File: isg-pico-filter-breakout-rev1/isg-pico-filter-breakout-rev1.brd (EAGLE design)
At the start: 91.4 x 66 mm, 51 parts, among them IC1 PICO_BAREDIE, U1 OPA2380AIDGKT, U2 OPA2380AIDGKT, U3 OPA2380AIDGKT, U4 OPA2380AIDGKT, U5 OPA2380AIDGKT, X3 PD_BIAS_N

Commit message: work on TIA layout
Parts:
- removed X3: PD_BIAS_N, con-coax:J502-ND-142-0701-881/886
- added JP1: (no value), pinhead:2X10
- added JP2: TIA_OUT, pinhead:2X10
- added R21, R22, R23, R24, R25, R26, R27, R28, R29, R30: RES SMD 49.9 OHM 1% 0603, rcl-modified-footprints:R0603
- added X1, X2: 1365-20, con-leotronics:1365-20
- moved H1 25.4 mm to (61.0, 19.1)
- moved H3 25.4 mm to (61.0, 47.0)
- moved H6 25.4 mm to (58.4, 7.62)
- moved H7 25.4 mm to (58.4, 58.4)
- moved R12 16.6 mm to (16.8, 56.2), turned to 270 degrees
- moved R11 16.2 mm to (16.8, 45.4), turned to 90 degrees
- moved R14 15.9 mm to (23.8, 56.2), turned to 270 degrees
- moved R13 15.6 mm to (23.8, 45.4), turned to 90 degrees
- moved R16 15.3 mm to (30.8, 56.2), turned to 270 degrees
- moved R15 15.0 mm to (30.8, 45.4), turned to 90 degrees
- moved R18 14.7 mm to (37.8, 56.2), turned to 270 degrees
- moved R17 14.3 mm to (37.8, 45.4), turned to 90 degrees
- moved R20 14.1 mm to (44.8, 56.2), turned to 270 degrees
- moved R1 14.1 mm to (19.1, 44.5)
- moved C1 14.0 mm to (19.1, 46.4)
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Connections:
- new net +5V: C12.1, C15.1, C3.1, C6.1, C9.1, JP1.19, U1.8, U2.8, U3.8, U4.8, U5.8
- new net -5V: JP1.1, R11.2, R12.2, R13.2, R14.2, R15.2, R16.2, R17.2, R18.2, R19.2, R20.2
- new net N$1: IC1.F1_H1_A, JP1.20
- new net N$10: IC1.F4_H1_A, JP1.2
- new net N$11: C4.2, R13.1, R23.1, R3.2, U2.1
- new net N$12: JP2.19, R21.2
- new net N$13: JP2.17, R22.2
- new net N$14: JP2.15, R23.2
- new net N$15: JP2.13, R24.2
- new net N$16: JP2.11, R25.2
- new net N$17: JP2.9, R26.2
- new net N$18: JP2.7, R27.2
- new net N$19: JP2.5, R28.2
- new net N$20: JP2.3, R29.2
- new net N$21: JP2.1, R30.2
- new net N$8: IC1.F4_H3_A, JP1.6
- new net N$9: IC1.F4_H2_A, JP1.4
- net F1_PD1_VOUT: now also R21.1
- net F2_PD1_VOUT: now also R22.1; no longer C4.2, R13.1, R3.2, U2.1
- net F3_PD1_VOUT: now also R26.1
- net F3_PD2_VOUT: now also R25.1
- net F3_PD3_VOUT: now also R24.1
- net F4_PD1_VOUT: now also R30.1
- net F4_PD2_VOUT: now also R29.1
- net F4_PD3_VOUT: now also R28.1
- net F4_PD4_VOUT: now also R27.1
- net GND: now also IC1.F1_H1_B, IC1.F2_H1_B, IC1.F2_H2_B, IC1.F3_H1_B, IC1.F3_H2_B, IC1.F3_H3_B, IC1.F4_H1_B, IC1.F4_H2_B, IC1.F4_H3_B, IC1.F4_H4_B, JP1.11, JP1.13, JP1.15, JP1.17, JP1.3, JP1.5, JP1.7, JP1.9, JP2.10, JP2.12, JP2.14, JP2.16, JP2.18, JP2.2, JP2.20, JP2.4, JP2.6, JP2.8; no longer X3.G@1, X3.G@2, X3.G@3, X3.G@4
- net N$2: now also IC1.F2_H2_A, JP1.18; no longer R11.2, R12.2
- net N$3: now also IC1.F2_H1_A, JP1.16; no longer R13.2, R14.2
- net N$4: now also IC1.F3_H3_A, JP1.14; no longer R15.2, R16.2
- net N$5: now also IC1.F3_H2_A, JP1.12; no longer R17.2, R18.2
- net N$6: now also IC1.F3_H1_A, JP1.10; no longer C12.1, C15.1, C3.1, C6.1, C9.1, U1.8, U2.8, U3.8, U4.8, U5.8
- net N$7: now also IC1.F4_H4_A, JP1.8; no longer R19.2, R20.2
- net PD_BIAS_N: no longer X3.1
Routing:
- net N$10: track 0.00 -> 24.3 mm
- net N$1: track 0.00 -> 24.0 mm
- net N$9: track 0.00 -> 23.3 mm
- net N$2: track 0.00 -> 23.0 mm
- net N$8: track 0.00 -> 22.4 mm
- net N$3: track 0.00 -> 22.1 mm
- net N$7: track 0.00 -> 21.5 mm
- net N$4: track 0.00 -> 21.5 mm
- net N$12: track 0.00 -> 21.1 mm
- net N$5: track 0.00 -> 20.6 mm
- net N$14: track 0.00 -> 19.2 mm
- net N$16: track 0.00 -> 17.3 mm
- net N$18: track 0.00 -> 16.1 mm
- net N$20: track 0.00 -> 15.4 mm
- net +5V: track 0.00 -> 14.3 mm
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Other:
- board size 91.4 x 66 mm -> 66 x 66 mm

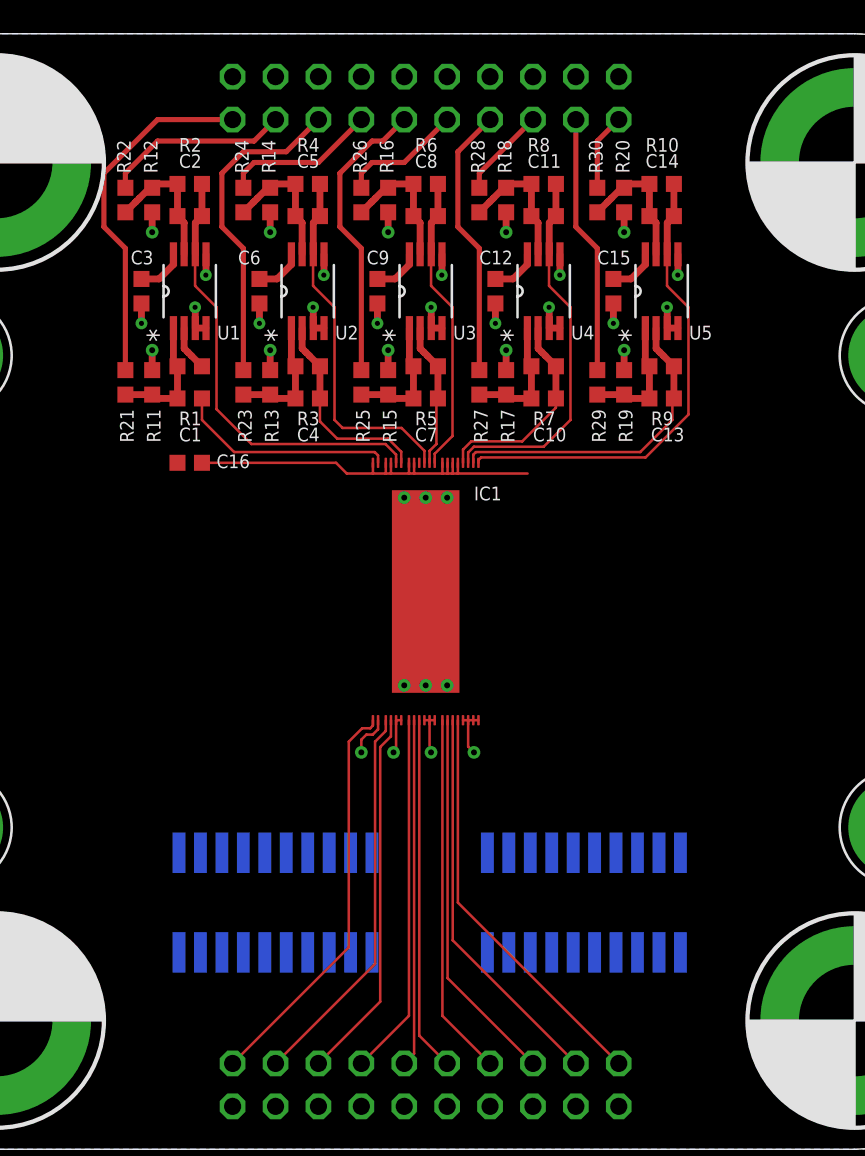
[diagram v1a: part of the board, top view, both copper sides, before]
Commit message: TIAs routed to 0.1" header
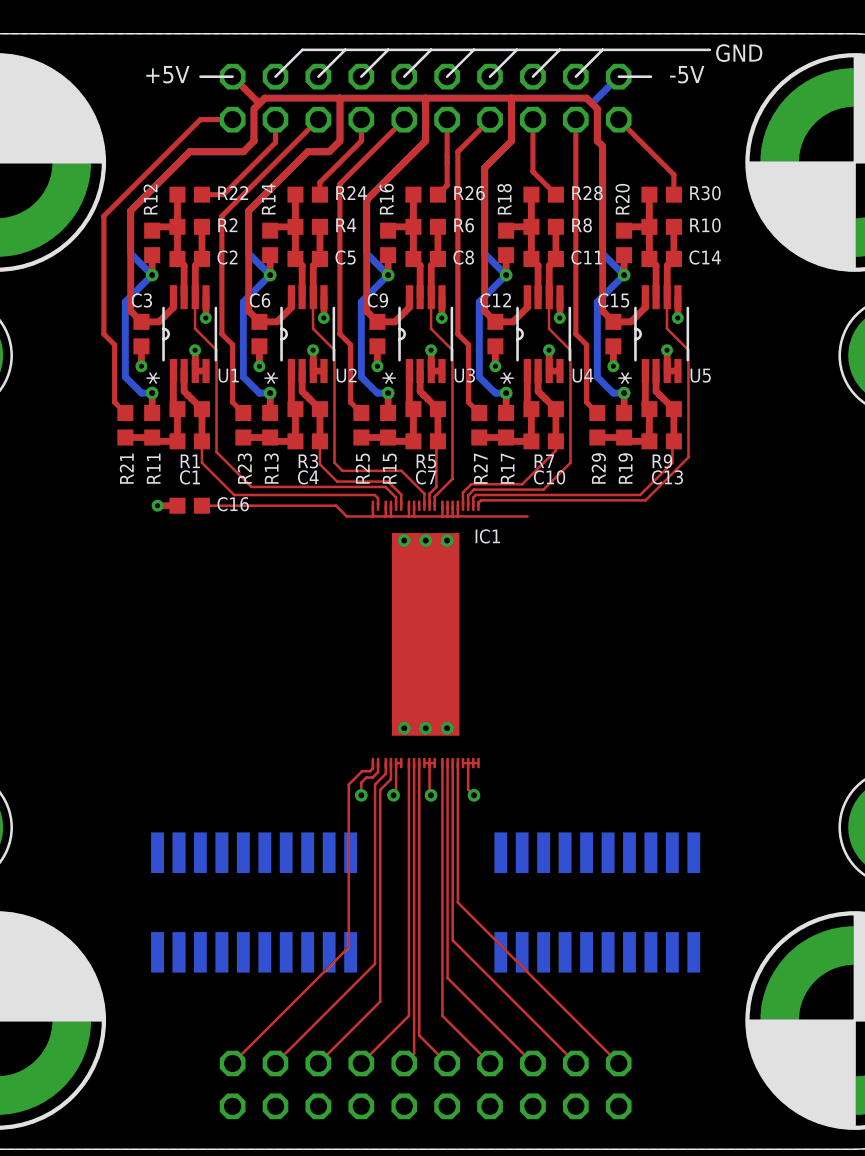
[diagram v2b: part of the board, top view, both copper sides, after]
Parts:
- moved R26 3.82 mm to (33.0, 56.5), turned to 0 degrees
- moved R28 3.82 mm to (40.0, 56.5), turned to 0 degrees
- moved R30 3.82 mm to (47.0, 56.5), turned to 0 degrees
- moved R22 3.82 mm to (19.1, 56.5), turned to 0 degrees
- moved R24 3.82 mm to (26.0, 56.5), turned to 0 degrees
- moved R1 2.54 mm to (19.1, 41.9)
- moved R11 2.54 mm to (16.8, 42.9)
- moved R13 2.54 mm to (23.8, 42.9)
- moved R15 2.54 mm to (30.8, 42.9)
- moved R17 2.54 mm to (37.8, 42.9)
- moved R19 2.54 mm to (44.8, 42.9)
- moved R21 2.54 mm to (15.2, 42.9)
- moved R23 2.54 mm to (22.2, 42.9)
- moved R25 2.54 mm to (29.2, 42.9)
- moved R27 2.54 mm to (36.2, 42.9)
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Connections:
- net N$12 renamed F1_PD1_VOUT_R
- net N$13 renamed F2_PD2_VOUT_R
- net N$14 renamed F2_PD1_VOUT_R
- net N$15 renamed F3_PD3_VOUT_R
- net N$16 renamed F3_PD2_VOUT_R
- net N$17 renamed F3_PD1_VOUT_R
- net N$18 renamed F4_PD4_VOUT_R
- net N$19 renamed F4_PD3_VOUT_R
- net N$20 renamed F4_PD2_VOUT_R
- net N$21 renamed F4_PD1_VOUT_R
- removed net N$11: C4.2, R13.1, R23.1, R3.2, U2.1
- new net F2_PD2_VOUT: C2.2, R12.1, R2.2, R22.1, U1.7
- net +5V: now also JP2.20; no longer JP1.19
- net -5V: now also JP2.2; no longer JP1.1
- net F2_PD1_VOUT: now also C4.2, R13.1, R23.1, R3.2, U2.1; no longer C2.2, R12.1, R2.2, R22.1, U1.7
- net GND: no longer JP2.2, JP2.20
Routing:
- net -5V: track 11.8 -> 142.1 mm
- net +5V: track 14.3 -> 113.7 mm
- net F2_PD2_VOUT: track 0.00 -> 7.96 mm
- net N$11: track 7.44 -> 0.00 mm
- net F2_PD2_VOUT_R: track 11.1 -> 6.99 mm
- net F3_PD3_VOUT_R: track 9.16 -> 5.46 mm
- net F3_PD1_VOUT_R: track 7.26 -> 4.67 mm
- net N$9: track 23.3 -> 20.8 mm
- net N$8: track 22.4 -> 19.9 mm
- net N$7: track 21.5 -> 18.9 mm
- net N$6: track 21.0 -> 18.5 mm
- net N$5: track 20.6 -> 18.0 mm
- net N$4: track 21.5 -> 18.9 mm
- net N$3: track 22.1 -> 19.6 mm
- net N$2: track 23.0 -> 20.5 mm
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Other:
- board text added: "+5V"
- board text added: "-5V"
- board text added: "GND"

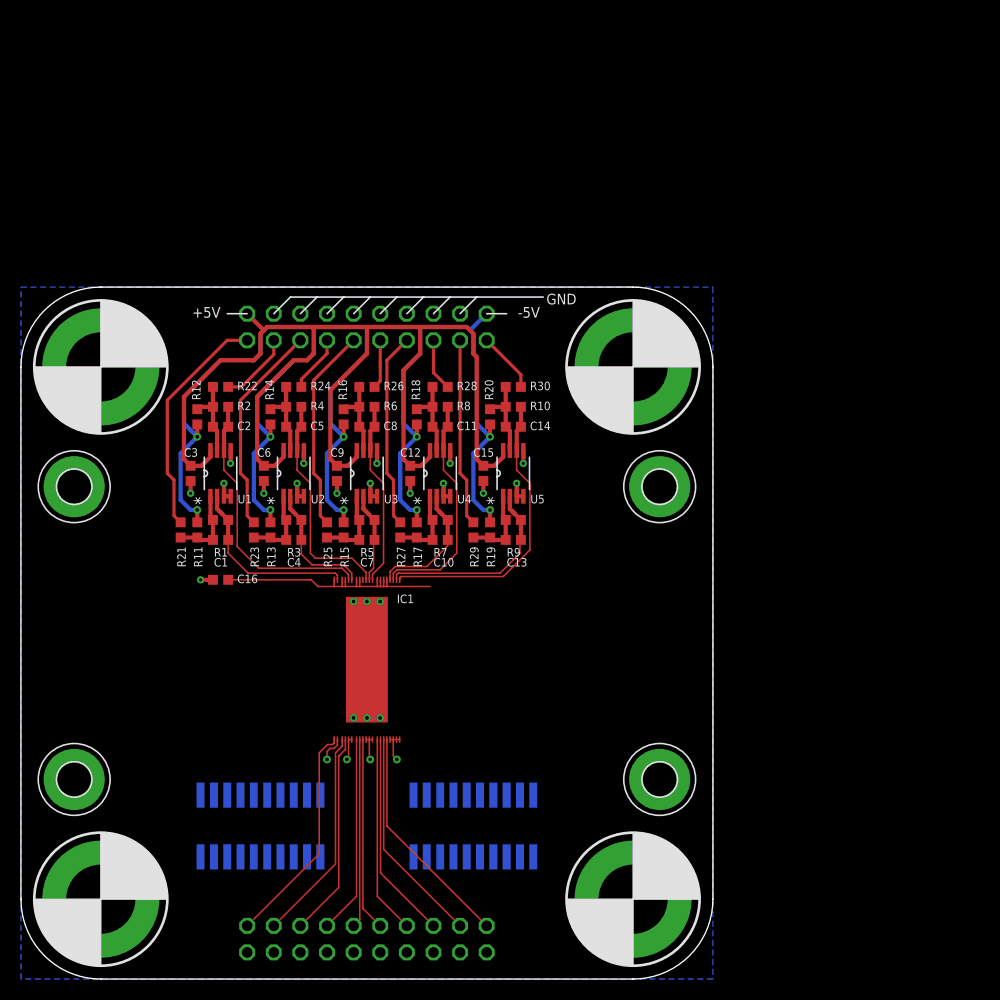
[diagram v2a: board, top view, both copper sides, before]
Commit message: first-pass routing done
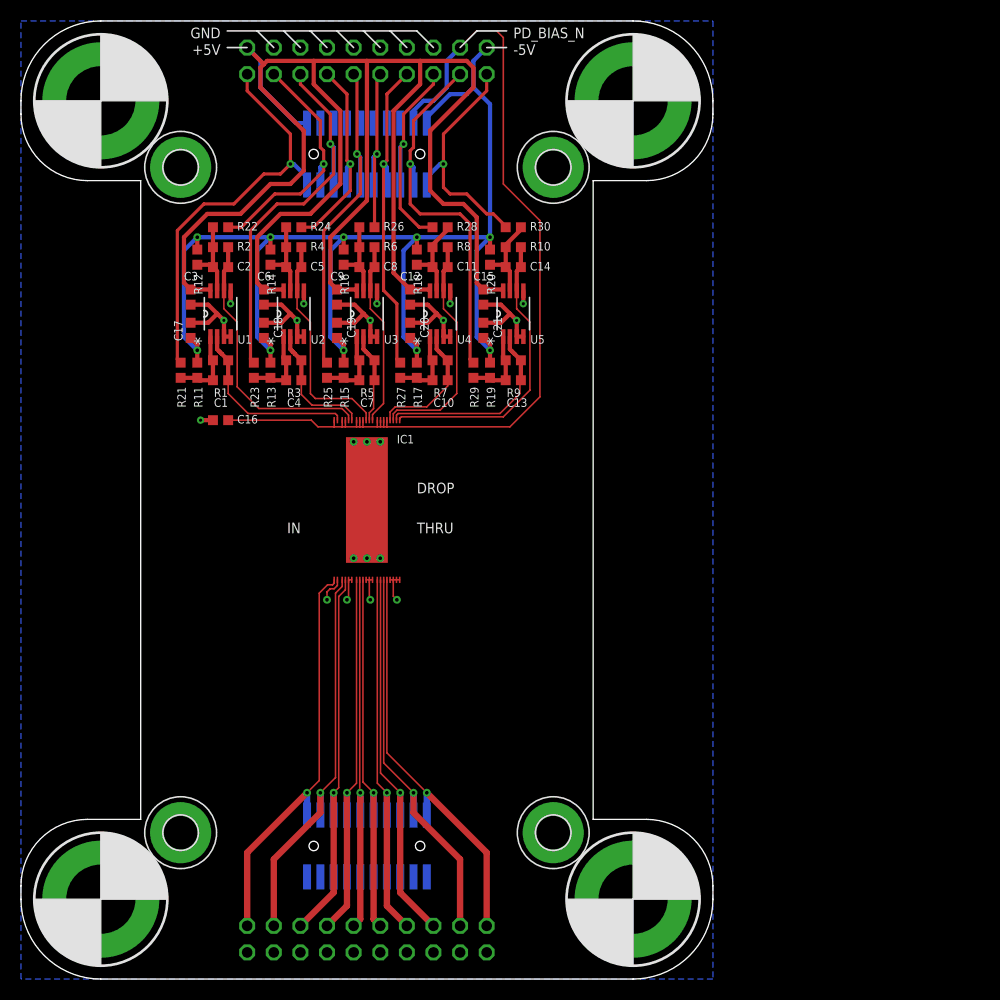
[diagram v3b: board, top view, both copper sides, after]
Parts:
- removed X1, X2: 1365-20, con-leotronics:1365-20
- added C17, C18, C19, C20, C21: CAP CER 0.1UF X7R 0603, rcl-modified-footprints:C0603
- added JP3, JP4: HEATERS, isg-custom:FTSH-110-01-L-DV-K-TR
- C12, C15, C16, C3, C6, C9: value CAP CER 100NF X7R 0603 -> CAP CER 0.1UF X7R 0603
- JP1: value (none) -> HEATERS
- moved H3 32.1 mm to (50.8, 77.5)
- moved H4 32.1 mm to (15.2, 77.5)
- moved JP2 25.4 mm to (33.0, 87.6)
- moved H7 25.4 mm to (58.4, 83.8)
- moved H8 25.4 mm to (7.62, 83.8)
- moved C12 16.8 mm to (37.1, 65.1)
- moved C15 16.8 mm to (44.1, 65.1)
- moved C3 16.8 mm to (16.2, 65.1)
- moved C6 16.8 mm to (23.2, 65.1)
- moved C9 16.8 mm to (30.2, 65.1)
- moved C1 15.2 mm to (19.1, 59.1)
- moved C10 15.2 mm to (40.0, 59.1)
- moved C13 15.2 mm to (47.0, 59.1)
- moved C16 15.2 mm to (19.1, 53.3)
- moved C4 15.2 mm to (26.0, 59.1)
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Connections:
- removed net N$1: IC1.F1_H1_A, JP1.20
- removed net N$10: IC1.F4_H1_A, JP1.2
- removed net N$2: IC1.F2_H2_A, JP1.18
- removed net N$3: IC1.F2_H1_A, JP1.16
- removed net N$4: IC1.F3_H3_A, JP1.14
- removed net N$5: IC1.F3_H2_A, JP1.12
- removed net N$6: IC1.F3_H1_A, JP1.10
- removed net N$7: IC1.F4_H4_A, JP1.8
- removed net N$8: IC1.F4_H3_A, JP1.6
- removed net N$9: IC1.F4_H2_A, JP1.4
- new net F1_H1_A: IC1.F1_H1_A, JP1.20, JP4.20
- new net F2_H1_A: IC1.F2_H1_A, JP1.16, JP4.16
- new net F2_H2_A: IC1.F2_H2_A, JP1.18, JP4.18
- new net F3_H1_A: IC1.F3_H1_A, JP1.10, JP4.10
- new net F3_H2_A: IC1.F3_H2_A, JP1.12, JP4.12
- new net F3_H3_A: IC1.F3_H3_A, JP1.14, JP4.14
- new net F4_H1_A: IC1.F4_H1_A, JP1.2, JP4.2
- new net F4_H2_A: IC1.F4_H2_A, JP1.4, JP4.4
- new net F4_H3_A: IC1.F4_H3_A, JP1.6, JP4.6
- new net F4_H4_A: IC1.F4_H4_A, JP1.8, JP4.8
- net +5V: now also JP3.1
- net -5V: now also C17.2, C18.2, C19.2, C20.2, C21.2, JP3.19
- net F1_PD1_VOUT_R: now also JP3.2
- net F2_PD1_VOUT_R: now also JP3.6
- net F2_PD2_VOUT_R: now also JP3.4
- net F3_PD1_VOUT_R: now also JP3.12
- net F3_PD2_VOUT_R: now also JP3.10
- net F3_PD3_VOUT_R: now also JP3.8
- net F4_PD1_VOUT_R: now also JP3.20
- net F4_PD2_VOUT_R: now also JP3.18
- net F4_PD3_VOUT_R: now also JP3.16
- net F4_PD4_VOUT_R: now also JP3.14
- net GND: now also C17.1, C18.1, C19.1, C20.1, C21.1, JP1.1, JP1.19, JP3.11, JP3.13, JP3.15, JP3.3, JP3.5, JP3.7, JP3.9, JP4.1, JP4.11, JP4.13, JP4.15, JP4.17, JP4.19, JP4.3, JP4.5, JP4.7, JP4.9; no longer JP2.4
- net PD_BIAS_N: now also JP2.4, JP3.17
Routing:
- net PD_BIAS_N: track 25.3 -> 87.9 mm
- net +5V: track 113.7 -> 175.1 mm
- net F4_H1_A: track 0.00 -> 39.1 mm, vias 0 -> 1
- net F1_H1_A: track 0.00 -> 38.9 mm, vias 0 -> 1
- net F4_H2_A: track 0.00 -> 38.2 mm, vias 0 -> 1
- net F2_H2_A: track 0.00 -> 37.9 mm, vias 0 -> 1
- net F4_H3_A: track 0.00 -> 37.2 mm, vias 0 -> 1
- net F2_H1_A: track 0.00 -> 36.9 mm, vias 0 -> 1
- net F4_H4_A: track 0.00 -> 36.3 mm, vias 0 -> 1
- net F3_H3_A: track 0.00 -> 36.3 mm, vias 0 -> 1
- net F3_H1_A: track 0.00 -> 35.8 mm, vias 0 -> 1
- net F3_H2_A: track 0.00 -> 35.4 mm, vias 0 -> 1
- net GND: track 32.9 -> 67.7 mm, vias 26 -> 21
- net N$10: track 21.7 -> 0.00 mm
- net N$1: track 21.5 -> 0.00 mm
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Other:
- board size 66 x 66 mm -> 66 x 91.4 mm
- board text added: "DROP"
- board text added: "IN"
- board text added: "PD_BIAS_N"
- board text added: "THRU"

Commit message: Added ESD diodes
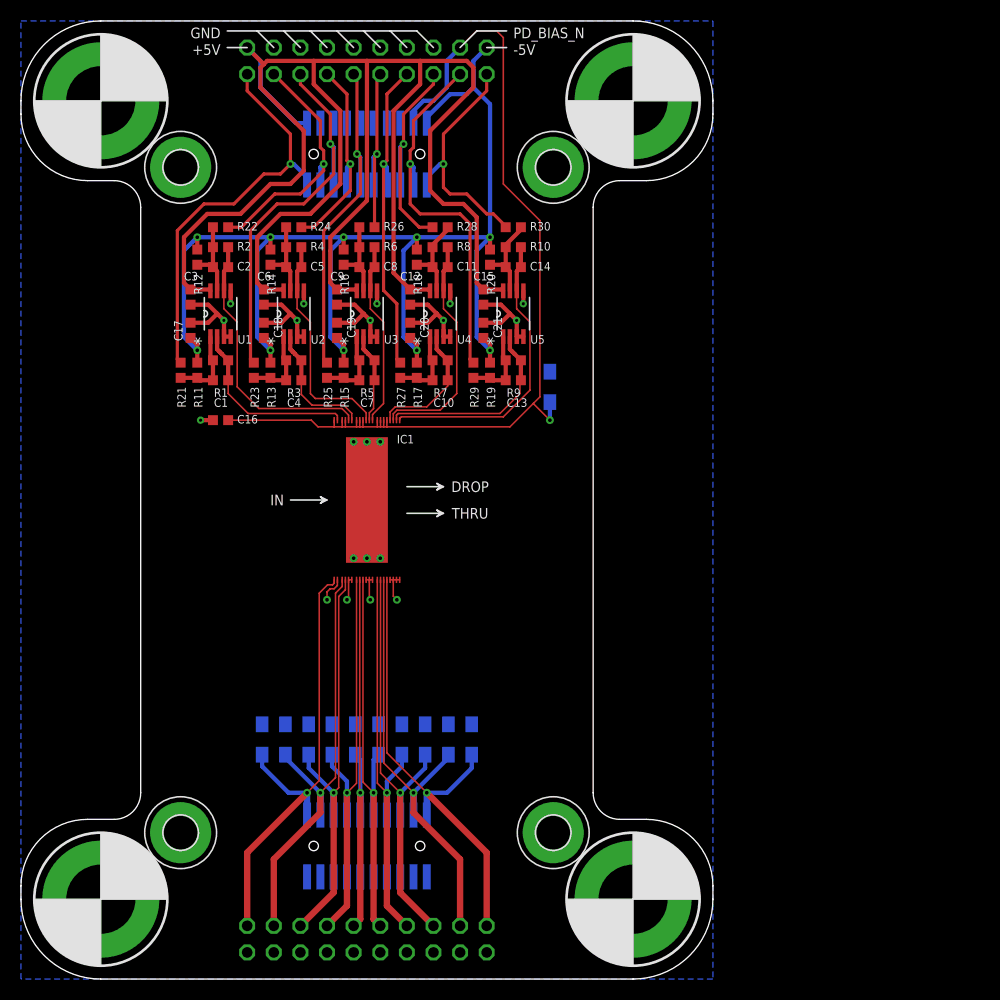
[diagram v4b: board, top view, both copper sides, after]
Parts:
- added D1, D10, D11, D2, D3, D4, D5, D6, D7, D8, D9: DF2B36FU,H3F, diode:SOD323-W
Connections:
- net F1_H1_A: now also D1.C
- net F2_H1_A: now also D4.C
- net F2_H2_A: now also D2.C
- net F3_H1_A: now also D7.C
- net F3_H2_A: now also D6.C
- net F3_H3_A: now also D5.C
- net F4_H1_A: now also D11.C
- net F4_H2_A: now also D10.C
- net F4_H3_A: now also D9.C
- net F4_H4_A: now also D8.C
- net GND: now also D1.A, D10.A, D11.A, D2.A, D3.C, D4.A, D5.A, D6.A, D7.A, D8.A, D9.A
- net PD_BIAS_N: now also D3.A
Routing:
- net F4_H1_A: track 39.1 -> 45.6 mm
- net F1_H1_A: track 38.9 -> 45.3 mm
- net F4_H2_A: track 38.2 -> 43.2 mm
- net F2_H2_A: track 37.9 -> 42.9 mm
- net F4_H3_A: track 37.2 -> 41.9 mm
- net F2_H1_A: track 36.9 -> 41.6 mm
- net F3_H3_A: track 36.3 -> 40.5 mm
- net F4_H4_A: track 36.3 -> 40.5 mm
- net PD_BIAS_N: track 87.9 -> 91.9 mm, vias 0 -> 1
- net F3_H1_A: track 35.8 -> 39.7 mm
- net F3_H2_A: track 35.4 -> 39.3 mm
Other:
- outline, holes or cut-outs redrawn
